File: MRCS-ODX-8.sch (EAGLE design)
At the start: 13 parts

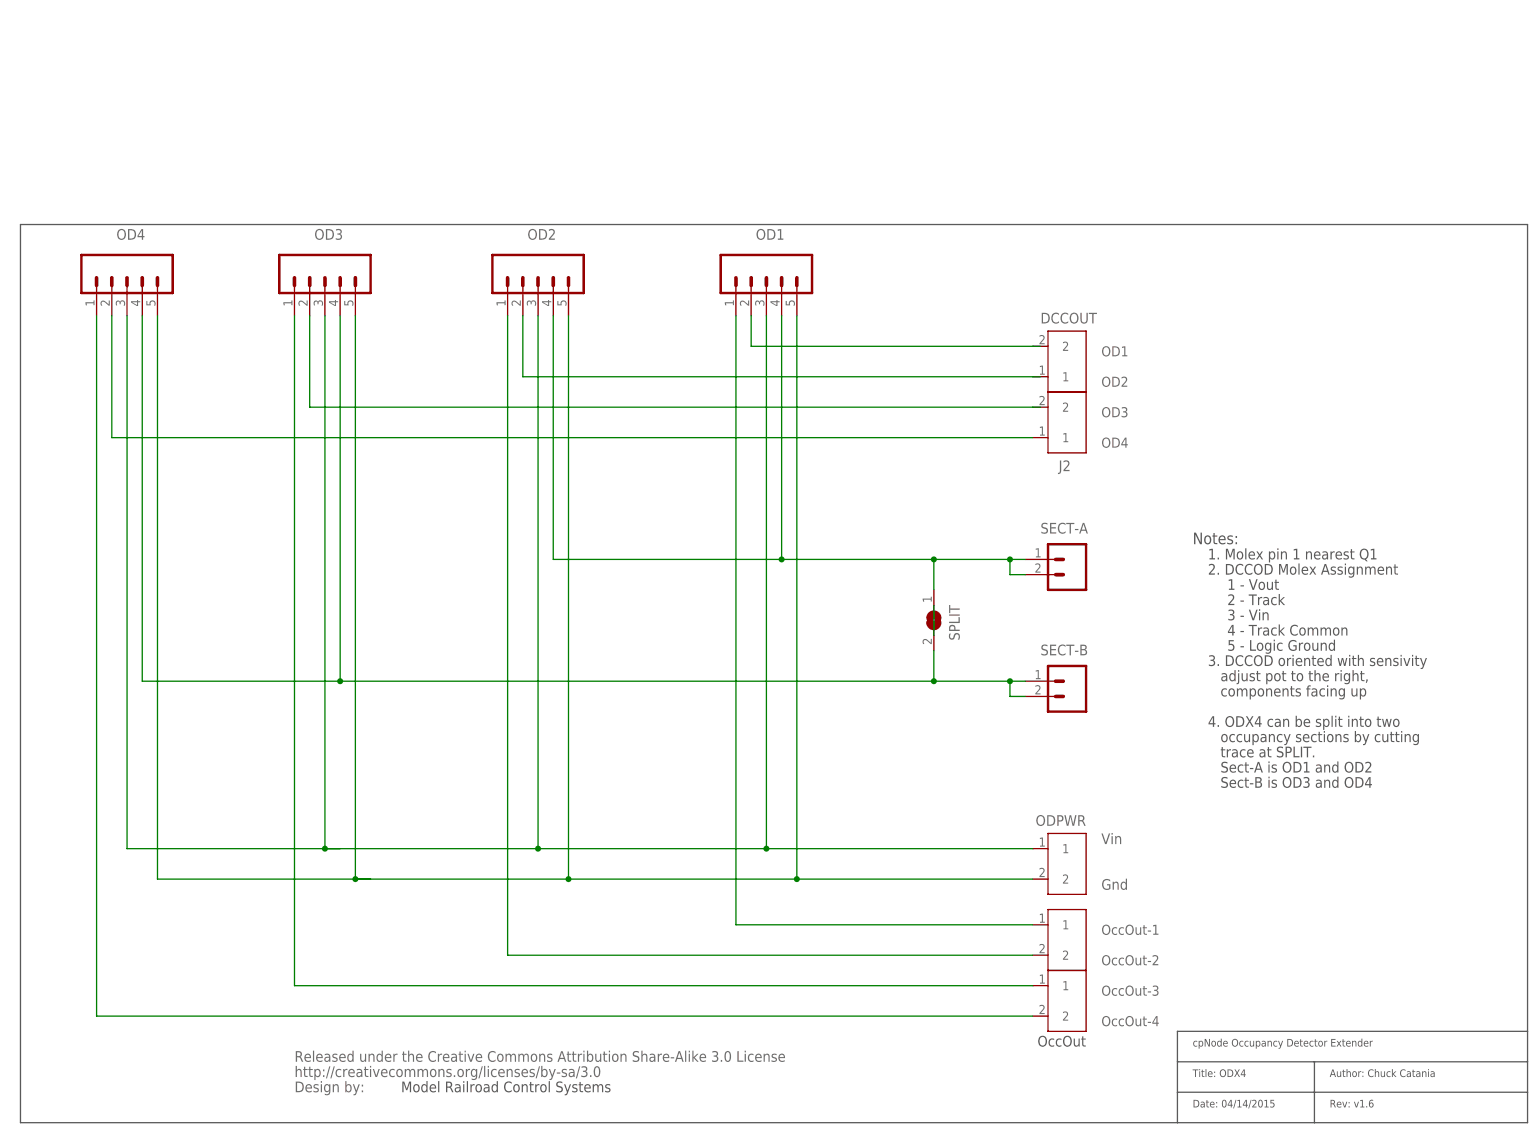
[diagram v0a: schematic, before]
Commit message: Release Zero 20210405
prototypes.  Silkscreen on 3 position screw terminal has Track Common and GND reversed, needs adjustment of OD7 and expand needs to be moved inwards.  Otherwise electrically OK.  Track common bus on bottom can be cleaned up.
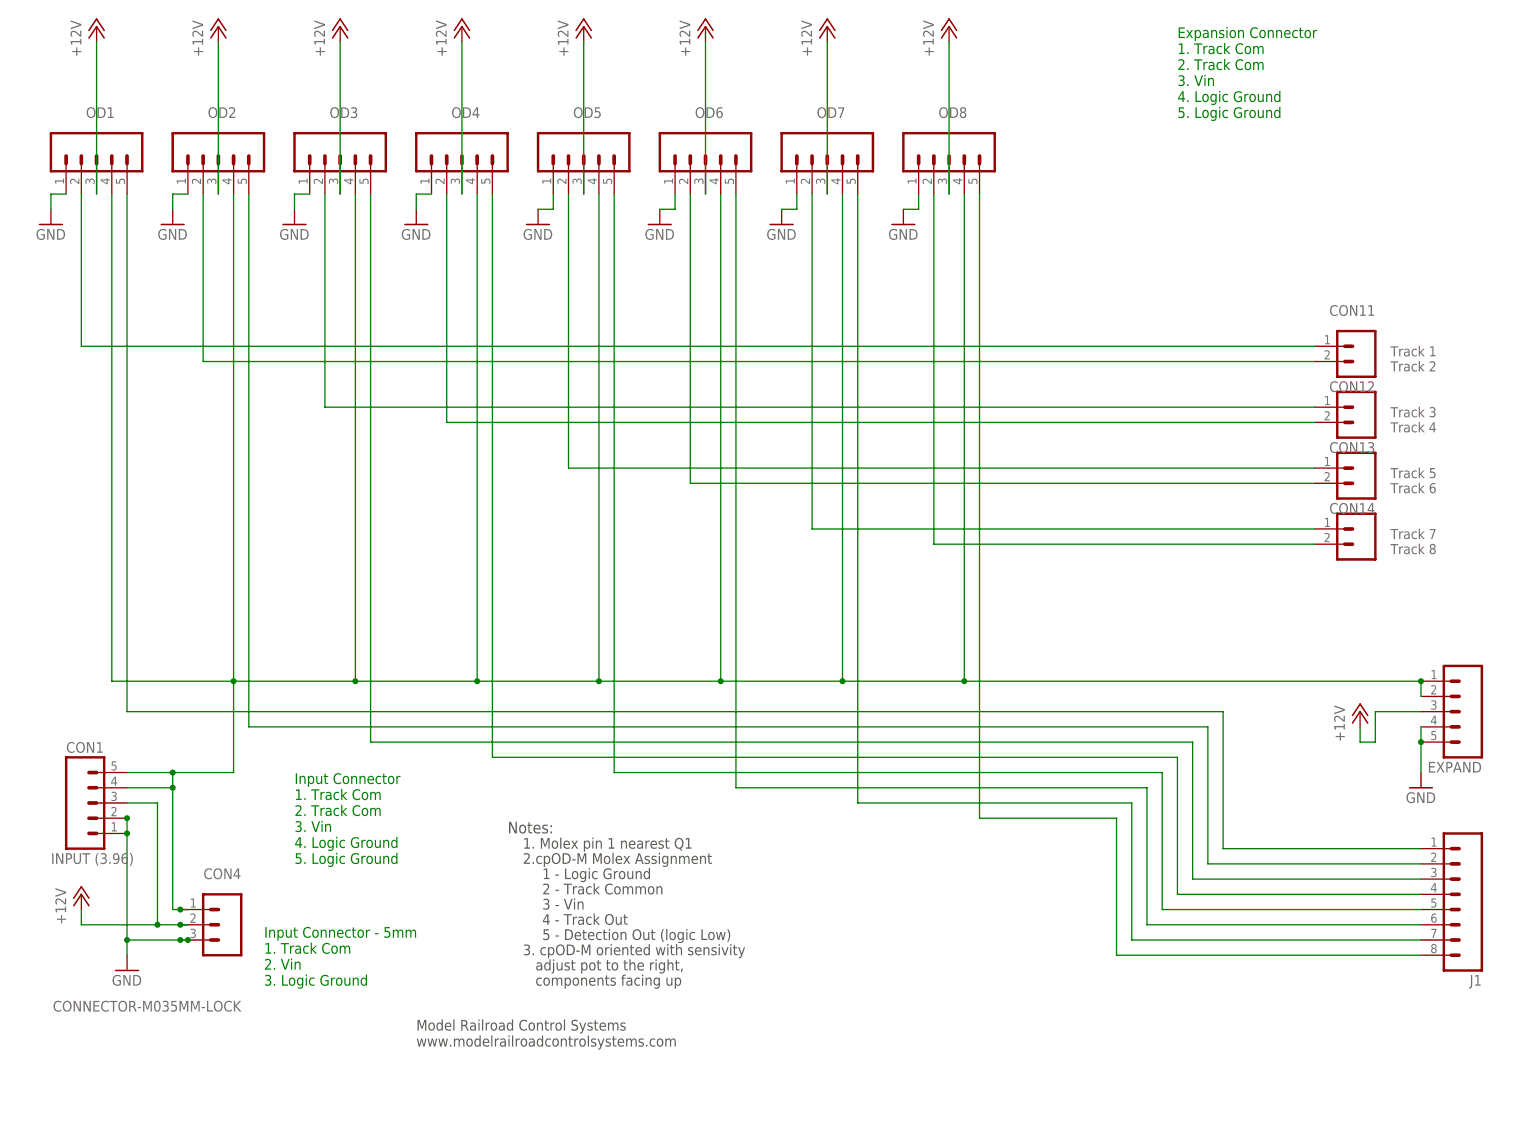
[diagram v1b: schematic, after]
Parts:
- removed DCCOUT, J2, ODPWR, ODXPWR1, ODXPWR2: (no value), Connector:SCREW-TERMINAL-2P
- removed SECT-A, SECT-B: M025MM, SparkFun-Connectors:M025MM
- removed SPLIT: (no value), jumper:SJW
- removed U$1: CREATIVE_COMMONS, SparkFun:CREATIVE_COMMONS
- added CON1: INPUT (3.96), SPCoast:CONNECTOR-M051.56
- added CON11, CON12, CON13, CON14: (no value), SPCoast:CONNECTOR-M025MM-LOCK
- added CON4: CONNECTOR-M035MM-LOCK, SPCoast:CONNECTOR-M035MM-LOCK
- added EXPAND, OD5, OD6, OD7, OD8: (no value), SPCoast:CONNECTOR-M051.56
- added J1: (no value), SPCoast:CONNECTOR-M08LOCK
- OD1, OD2, OD3, OD4: device SparkFun:M05PTH_LONGPADS -> SPCoast:CONNECTOR-M051.56
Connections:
- removed net N$12: OD1.4, OD2.4, SECT-A.1, SECT-A.2, SPLIT.1
- removed net N$14: J2.2, OD3.2
- removed net N$2: OD1.1, ODXPWR1.1
- removed net N$4: DCCOUT.1, OD2.2
- removed net N$9: OD2.1, ODXPWR1.2
- new net +12V: CON1.3, CON4.2, EXPAND.3, OD1.3, OD2.3, OD3.3, OD4.3, OD5.3, OD6.3, OD7.3, OD8.3
- new net GND: CON1.1, CON1.2, CON4.3, EXPAND.4, EXPAND.5, OD1.1, OD2.1, OD3.1, OD4.1, OD5.1, OD6.1, OD7.1, OD8.1
- new net N$16: J1.6, OD6.5
- new net N$17: J1.8, OD8.5
- new net N$18: J1.7, OD7.5
- new net N$20: J1.3, OD3.5
- new net N$25: CON14.A, OD7.2
- new net N$26: CON12.B, OD4.2
- new net N$27: CON12.A, OD3.2
- new net N$28: CON11.B, OD2.2
- new net TRACK_POWER: CON1.4, CON1.5, CON4.1, EXPAND.1, EXPAND.2, OD1.4, OD2.4, OD3.4, OD4.4, OD5.4, OD6.4, OD7.4, OD8.4
- net N$1: now also CON14.B, OD8.2; no longer J2.1, OD4.2
- net N$10: now also J1.2, OD2.5; no longer ODXPWR2.2
- net N$11: now also J1.1, OD1.5; no longer OD3.4, OD4.4, SECT-B.1, SECT-B.2, SPLIT.2
- net N$13: now also J1.4, OD4.5; no longer OD4.1
- net N$15: now also J1.5, OD5.5; no longer OD1.3, OD2.3, OD3.3, OD4.3, ODPWR.1
- net N$3: now also CON11.A; no longer DCCOUT.2
- net N$5: now also CON13.B, OD6.2; no longer OD3.1, ODXPWR2.1
- net N$6: now also CON13.A, OD5.2; no longer OD1.5, OD2.5, OD3.5, OD4.5, ODPWR.2
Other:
- note added: "1 - Logic Ground"
- note added: "2 - Track Common"
- note added: "2.cpOD-M Molex Assignment"
- note added: "3. cpOD-M oriented with sensivity"
- note added: "4 - Track Out"
- note added: "5 - Detection Out (logic Low)"
- note added: "Expansion Connector 1. Track Com 2. Track Com 3. Vin 4. Logic Ground 5. Logic Ground"
- note added: "Input Connector - 5mm 1. Track Com 2. Vin 3. Logic Ground"
- note added: "Input Connector 1. Track Com 2. Track Com 3. Vin 4. Logic Ground 5. Logic Ground"
- note added: "Model Railroad Control Systems www.modelrailroadcontrolsystems.com"
- note added: "Track 1 Track 2"
- note added: "Track 3 Track 4"
- note added: "Track 5 Track 6"
- note added: "Track 7 Track 8"
- note removed: "1 - Vout"
- note removed: "2 - Track"
- note removed: "2. DCCOD Molex Assignment"
- note removed: "3. DCCOD oriented with sensivity"
- note removed: "4 - Track Common"
- note removed: "4. ODX4 can be split into two"
- note removed: "5 - Logic Ground"
- note removed: "Author: Chuck Catania"
- note removed: "Date: 04/14/2015"
- note removed: "Gnd"
- note removed: "Model Railroad Control Systems"
- note removed: "OD1"
- note removed: "OD2"
- note removed: "OD3"
- note removed: "OD4"
- note removed: "OccOut"
- note removed: "OccOut-1"
- note removed: "OccOut-2"
- note removed: "OccOut-3"
- note removed: "OccOut-4"
- note removed: "Rev: v1.6"
- note removed: "Sect-A is OD1 and OD2"
- note removed: "Sect-B is OD3 and OD4"
- note removed: "Title: ODX4"
- note removed: "Vin"
- note removed: "cpNode Occupancy Detector Extender"
- note removed: "occupancy sections by cutting"
- note removed: "trace at SPLIT."
